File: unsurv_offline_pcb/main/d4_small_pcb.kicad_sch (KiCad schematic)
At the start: 59 parts, among them J1 U_FL-R-SMT-1_10_, J2 S2B-PH-SM4-TB_LF__SN_, Q1 UMH3N, U1 TTGO-Micro32-ESP32, U2 RF430CL330HIRGTR‎, U3 CAM-M8C-0-10, U4 AP2112K-3.3, U5 CH340G, U6 BQ25180, U7 BMA400-I2C, U8 RFM95W-868S2

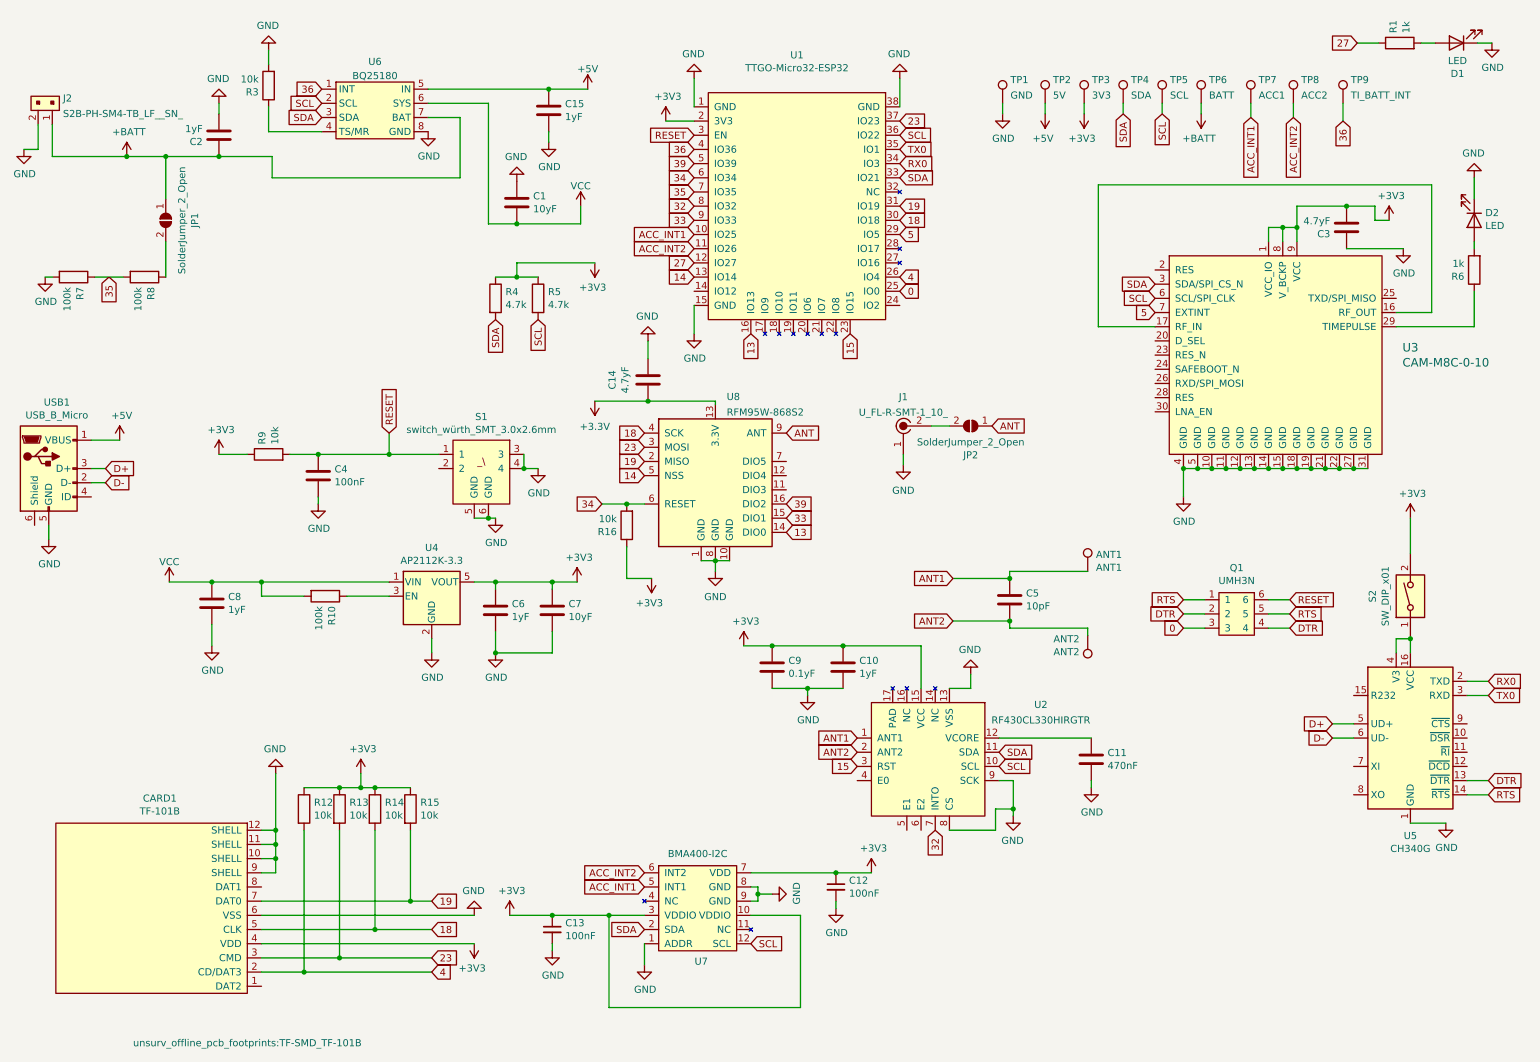
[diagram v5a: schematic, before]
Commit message: remove hand soldering footprints
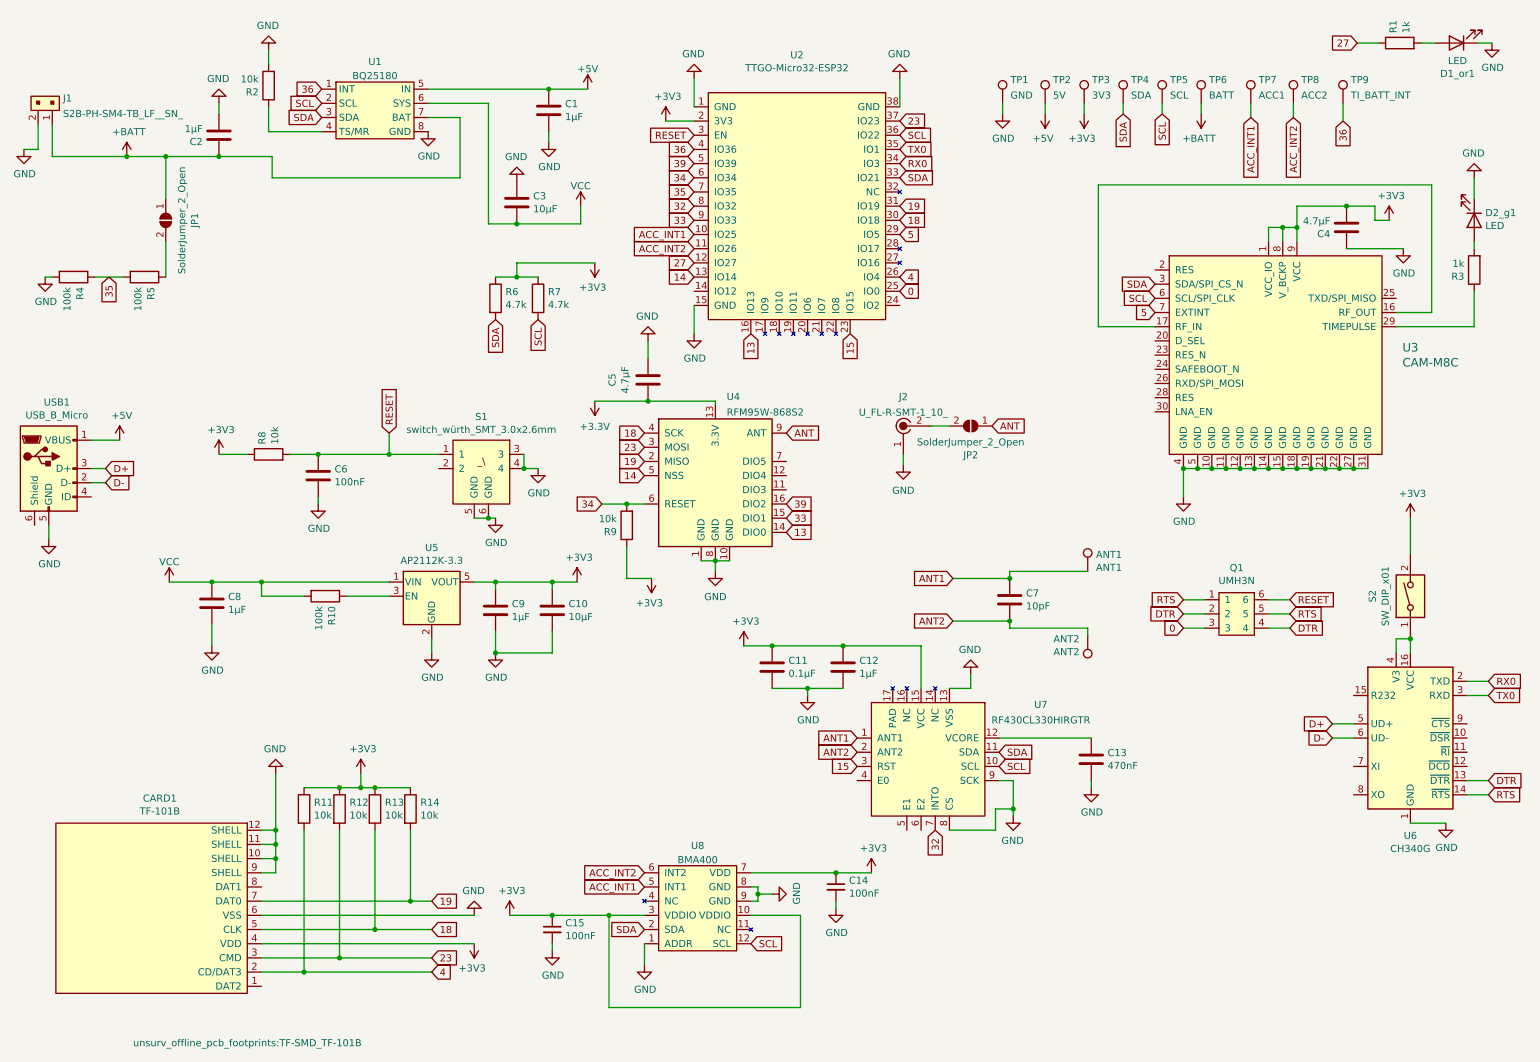
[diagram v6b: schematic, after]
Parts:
- removed U7: BMA400-I2C, unsurv_offline_pcb_footprints:BMA400_regular, symbol unsurv_offline_pcb_symbols:BMA400-I2C
- added U8: BMA400, unsurv_offline_pcb_footprints:BMA400_regular, symbol unsurv_offline_pcb_symbols:BMA400
- ANT1, ANT2: MFG (none) -> Harwin; MPN (none) -> P70-1010045R
- C1: renamed from C15; value 1yF -> 1µF
- C10: renamed from C7; value 10yF -> 10µF
- C11: renamed from C9; value 0.1yF -> 0.1µF
- C12: renamed from C10; value 1yF -> 1µF
- C13: renamed from C11; MFG (none) -> Murata Electronics; MFN (none) -> GRM188R61E474KA12D
- C2, C8: value 1yF -> 1µF
- C3: renamed from C1; value 10yF -> 10µF
- C4: renamed from C3; value 4.7yF -> 4.7µF
- C5: renamed from C14; value 4.7yF -> 4.7µF
- C7: renamed from C5; MFG (none) -> Murata Electronics; MFN (none) -> GCM1885C2A100FA16J
- C9: renamed from C6; value 1yF -> 1µF
- CARD1: MPN (none) -> TF-101B; OC_LCSC (none) -> C266608
- D1_or1: renamed from D1; MFG (none) -> Kingbright; MFN (none) -> APHD1608LSURCK
- D2_g1: renamed from D2; MFG (none) -> Kingbright; MFN (none) -> APTD1608LCGCK
- S1: MFG (none) -> Wurth Elektronik; MPN (none) -> 435171014816
- S2: MFG (none) -> Nidec Components; MPN (none) -> CHS-01TA
- U1: renamed from U6; MFG (none) -> Texas Instruments; MPN (none) -> BQ25180YBGR
- U3: value CAM-M8C-0-10 -> CAM-M8C
- U5: renamed from U4; MFG (none) -> Diodes Incorporated; MFN (none) -> AP2112K-3.3TRG1
- U6: renamed from U5; MFN (none) -> CH340G; OC_LCSC (none) -> C14267
- U7: renamed from U2; MFG (none) -> Texas Instruments; MPN (none) -> RF430CL330HIRGTR
- USB1: MFG (none) -> Amphenol FCI; MPN (none) -> 10103594-0001LF
- renumbered C12 to C14, C13 to C15, C4 to C6, J2 to J1, J1 to J2, R12 to R11, R13 to R12, R14 to R13, R15 to R14, R3 to R2, R6 to R3, R7 to R4, R8 to R5, R4 to R6, R5 to R7, R9 to R8, R16 to R9, U1 to U2, U8 to U4
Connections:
- net +3V3: now also U8.10 (VDDIO), U8.3 (VDDIO), U8.7 (VDD)
- net ACC_INT1: now also U8.5 (INT1)
- net ACC_INT2: now also U8.6 (INT2)
- net GND: now also U8.1 (ADDR), U8.8 (GND), U8.9 (GND)
- net SCL: now also U8.12 (SCL)
- net SDA: now also U8.2 (SDA)

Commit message: certification test
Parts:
- D1_or1: value LED -> LED1
- D2_g1: value LED -> LED2

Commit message: new footprints
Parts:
- added C5: 10µF, Capacitor_SMD:C_0603_1608Metric, symbol Device:C
- added L1, L2: L_Ferrite, Inductor_SMD:L_0603_1608Metric, symbol Device:L_Ferrite
- renumbered C9 to C10, C10 to C11, C11 to C12, C12 to C13, C13 to C14, C14 to C15, C15 to C16, C5 to C6, C6 to C7, C7 to C8, C8 to C9
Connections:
- net +3V3: now also C5.1, L2.1
- net +5V: now also L1.1
- net GND: now also C5.2, L1.2, L2.2
